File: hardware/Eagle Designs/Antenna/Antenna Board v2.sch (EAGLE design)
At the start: 12 parts, among them J1 503763-0591, J10 U.FL-R-SMT-1(01), J2 MOLEX_503763-0491MOLEX_503763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, J3 MOLEX_503763-0491MOLEX_503763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, J4 MOLEX_503763-0291MOLEX_503763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, J5 503763-0591, J6 MOLEX_503763-0491MOLEX_503763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, J7 MOLEX_503763-0491MOLEX_503763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, J8 MOLEX_503763-0291MOLEX_503763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, J9 MOLEX_503763-0291MOLEX_503763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

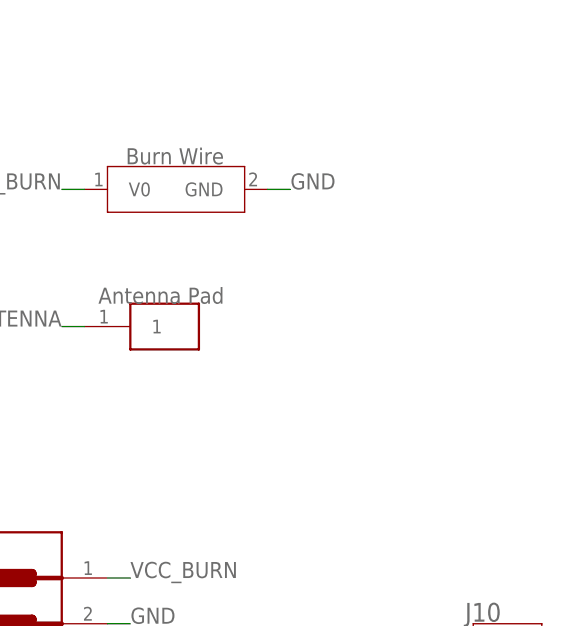
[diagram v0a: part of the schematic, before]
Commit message: Updated antenna and solar panel boards.
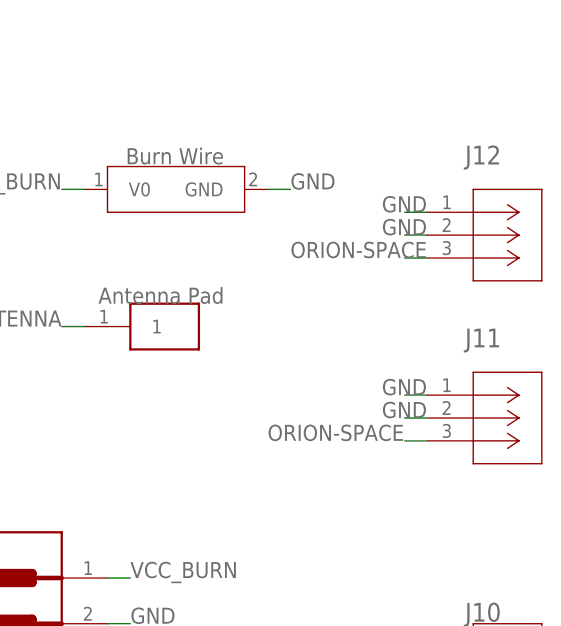
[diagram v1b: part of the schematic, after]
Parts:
- added J11, J12: U.FL-R-SMT-1(01), U.FL-R-SMT:U.FL-R-SMT-1(01)
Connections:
- new net ORION-SPACE: J11.3, J12.3
- net GND: now also J11.1, J11.2, J12.1, J12.2
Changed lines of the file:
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@@
 <part name="U$2" library="Antenna_Pad" deviceset="ANTENNA_PAD" device=""/>
 <part name="U$3" library="Burn_Wire" deviceset="BURNWIRE" device=""/>
+<part name="J11" library="U.FL-R-SMT" deviceset="U.FL-R-SMT-1(01)" device=""/>
+<part name="J12" library="U.FL-R-SMT" deviceset="U.FL-R-SMT-1(01)" device=""/>
 </parts>
 <sheets>
@@
 <instance part="U$2" gate="G$1" x="185.42" y="66.04" smashed="yes"/>
 <instance part="U$3" gate="G$1" x="185.42" y="83.82" smashed="yes"/>
+<instance part="J11" gate="A" x="220.98" y="63.5" smashed="yes">
+<attribute name="NAME" x="225.1456" y="68.8086" size="2.0828" layer="95" ratio="6" rot="SR0"/>
+</instance>
+<instance part="J12" gate="A" x="220.98" y="83.82" smashed="yes">
+<attribute name="NAME" x="225.1456" y="89.1286" size="2.0828" layer="95" ratio="6" rot="SR0"/>
+</instance>
 </instances>
 <busses>
@@
 <pinref part="U$3" gate="G$1" pin="GND"/>
 </segment>
-</net>
+<segment>
+<pinref part="J12" gate="A" pin="1"/>
+<wire x1="220.98" y1="83.82" x2="218.44" y2="83.82" width="0.1524" layer="91"/>
+<label x="215.9" y="83.82" size="1.778" layer="95"/>
+</segment>
+<segment>
+<pinref part="J12" gate="A" pin="2"/>
+<wire x1="220.98" y1="81.28" x2="218.44" y2="81.28" width="0.1524" layer="91"/>
+<label x="215.9" y="81.28" size="1.778" layer="95"/>
+</segment>
+<segment>
+<pinref part="J11" gate="A" pin="1"/>
+<wire x1="220.98" y1="63.5" x2="218.44" y2="63.5" width="0.1524" layer="91"/>
+<label x="215.9" y="63.5" size="1.778" layer="95"/>
+</segment>
+<segment>
+<pinref part="J11" gate="A" pin="2"/>
+<wire x1="220.98" y1="60.96" x2="218.44" y2="60.96" width="0.1524" layer="91"/>
+<label x="215.9" y="60.96" size="1.778" layer="95"/>
+</segment>
+</net>
+<net name="ORION-SPACE" class="0">
+<segment>
+<pinref part="J12" gate="A" pin="3"/>
+<wire x1="220.98" y1="78.74" x2="218.44" y2="78.74" width="0.1524" layer="91"/>
+<label x="205.74" y="78.74" size="1.778" layer="95"/>
+</segment>
+<segment>
+<pinref part="J11" gate="A" pin="3"/>
+<wire x1="220.98" y1="58.42" x2="218.44" y2="58.42" width="0.1524" layer="91"/>
+<label x="203.2" y="58.42" size="1.778" layer="95"/>
+</segment>
+</net>

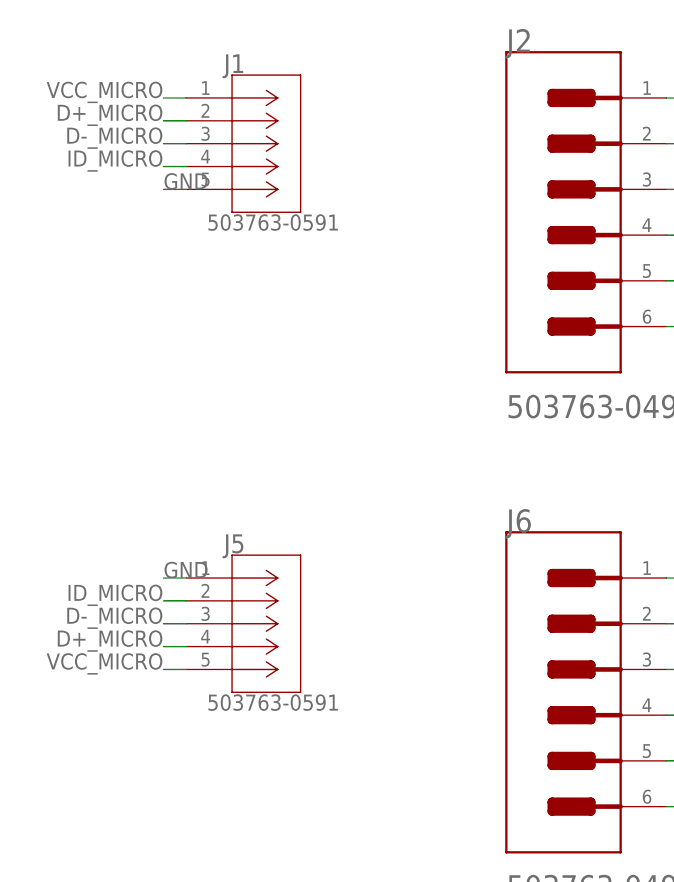
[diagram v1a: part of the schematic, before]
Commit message: Updated antenna and solar panel boards
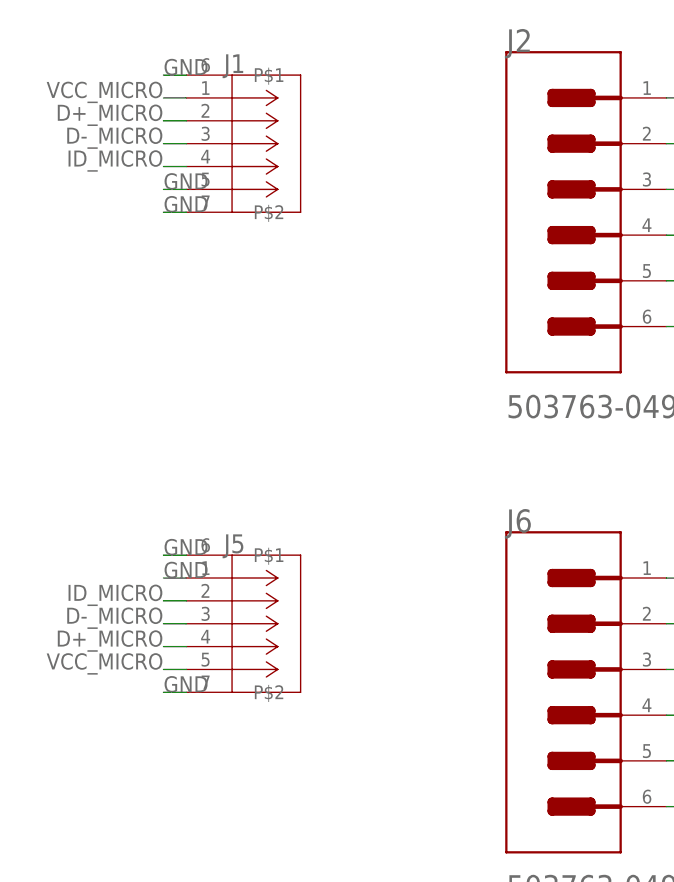
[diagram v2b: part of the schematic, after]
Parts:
- J1, J5: device Molex - 503763-0591:503763-0591 -> Improved Molex 503763-0591:503763-0591
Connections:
- net GND: now also J1.P$1, J1.P$2, J5.P$1, J5.P$2
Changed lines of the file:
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@@
 <part name="J2" library="Molex - 503763-0491" deviceset="MOLEX_503763-0491" device="MOLEX_503763-0491_0_0"/>
 <part name="J3" library="Molex - 503763-0491" deviceset="MOLEX_503763-0491" device="MOLEX_503763-0491_0_0"/>
-<part name="J1" library="Molex - 503763-0591" deviceset="503763-0591" device=""/>
+<part name="J1" library="Improved Molex 503763-0591" deviceset="503763-0591" device=""/>
 <part name="J10" library="U.FL-R-SMT-1(01)" deviceset="U.FL-R-SMT-1(01)" device=""/>
 <part name="J8" library="Molex - 503763-0291" deviceset="MOLEX_503763-0291" device="MOLEX_503763-0291_0_0"/>
 <part name="J6" library="Molex - 503763-0491" deviceset="MOLEX_503763-0491" device="MOLEX_503763-0491_0_0"/>
 <part name="J7" library="Molex - 503763-0491" deviceset="MOLEX_503763-0491" device="MOLEX_503763-0491_0_0"/>
-<part name="J5" library="Molex - 503763-0591" deviceset="503763-0591" device=""/>
+<part name="J5" library="Improved Molex 503763-0591" deviceset="503763-0591" device=""/>
 <part name="U$2" library="Antenna_Pad" deviceset="ANTENNA_PAD" device=""/>
 <part name="U$3" library="Burn_Wire" deviceset="BURNWIRE" device=""/>
@@
 <label x="215.9" y="60.96" size="1.778" layer="95"/>
 </segment>
-</net>
+<segment>
+<pinref part="J1" gate="A" pin="P$2"/>
+<wire x1="15.24" y1="83.82" x2="12.7" y2="83.82" width="0.1524" layer="91"/>
+<label x="12.7" y="83.82" size="1.778" layer="95"/>
+</segment>
+<segment>
+<pinref part="J1" gate="A" pin="P$1"/>
+<wire x1="15.24" y1="99.06" x2="12.7" y2="99.06" width="0.1524" layer="91"/>
+<label x="12.7" y="99.06" size="1.778" layer="95"/>
+</segment>
+<segment>
+<pinref part="J5" gate="A" pin="P$2"/>
+<wire x1="15.24" y1="30.48" x2="12.7" y2="30.48" width="0.1524" layer="91"/>
+<label x="12.7" y="30.48" size="1.778" layer="95"/>
+</segment>
+<segment>
+<pinref part="J5" gate="A" pin="P$1"/>
+<wire x1="15.24" y1="45.72" x2="12.7" y2="45.72" width="0.1524" layer="91"/>
+<label x="12.7" y="45.72" size="1.778" layer="95"/>
+</segment>
+</net>
